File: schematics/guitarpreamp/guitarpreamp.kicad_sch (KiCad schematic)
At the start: 49 parts, among them J1 10k Pot, J10 Conn_01x01_Female, J11 Conn_01x01_Female, J2 Conn_01x08_Female, J3 Conn_01x05_Female, J4 Conn_01x03_Female, U1 9V Linear Regulator, U2 TL072, U3 5V Linear Regulator, U4 3.3v Digital, U5 5v Analog, U6 CS4270-CZZ, X1 SG-5032CAN

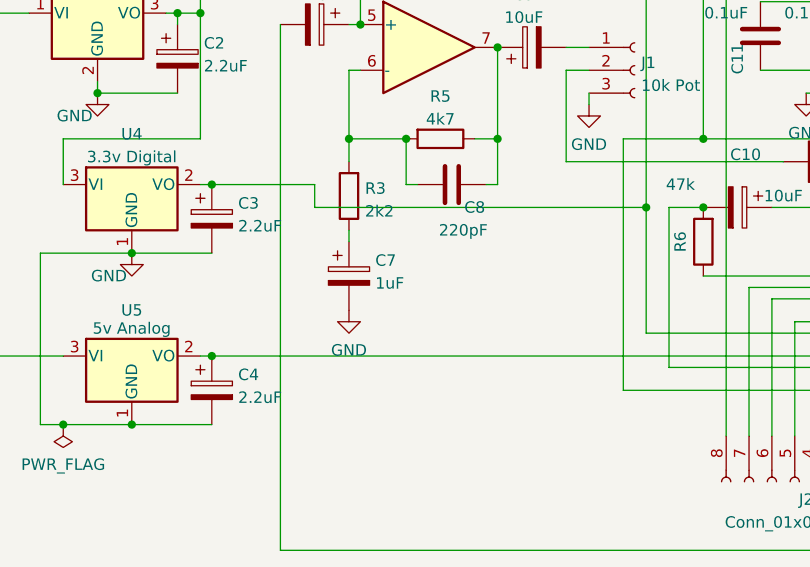
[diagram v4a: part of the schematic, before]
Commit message: changed cab values
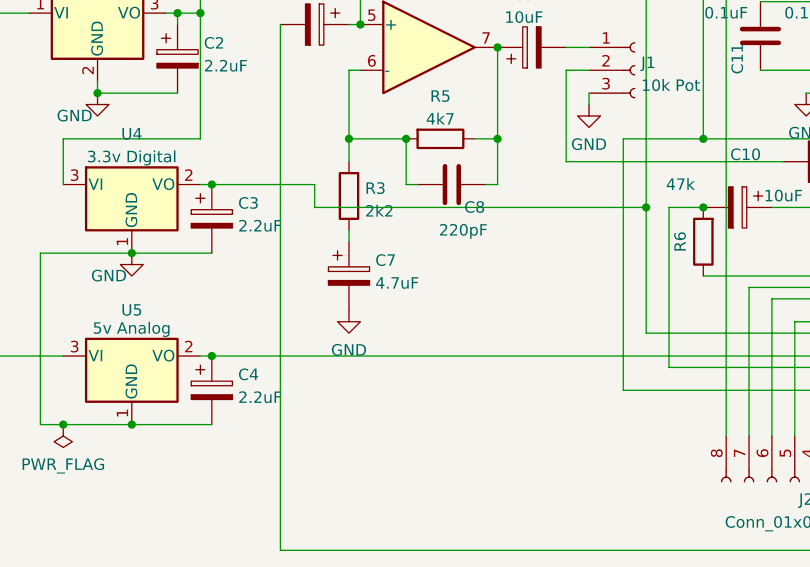
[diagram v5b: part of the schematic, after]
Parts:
- C7: value 1uF -> 4.7uF
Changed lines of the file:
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@@
       (effects (font (size 1.27 1.27)) hide)
     )
-    (pin "1")
-    (pin "2")
-    (pin "3")
-    (pin "5")
-    (pin "6")
-    (pin "7")
     (pin "4")
     (pin "8")
@@
       (effects (font (size 1.27 1.27)) hide)
     )
-    (pin "1")
-    (pin "2")
-    (pin "3")
     (pin "5")
     (pin "6")
     (pin "7")
-    (pin "4")
-    (pin "8")
   )
   (symbol (lib_id "Amplifier_Operational:TL072") (at 90.17 49.53 0) (unit 1)
@@
     (pin "2")
     (pin "3")
-    (pin "5")
-    (pin "6")
-    (pin "7")
-    (pin "4")
-    (pin "8")
   )
   (symbol (lib_id "Device:C_Polarized") (at 233.68 92.71 180) (unit 1)
@@
       (effects (font (size 1.27 1.27)) (justify left))
     )
-    (property "Value" "1uF" (id 1) (at 85.471 101.1432 0)
+    (property "Value" "4.7uF" (id 1) (at 85.471 101.1432 0)
       (effects (font (size 1.27 1.27)) (justify left))
     )
@@
     )
     (path "/cf02f18a-afda-4ef9-b82e-96f662488231"
-      (reference "C7") (unit 1) (value "1uF") (footprint "Capacitor_SMD:CP_Elec_4x4.5")
+      (reference "C7") (unit 1) (value "4.7uF") (footprint "Capacitor_SMD:CP_Elec_4x4.5")
     )
     (path "/5e84eb23-316a-48ca-94bf-3d421a04b84d"

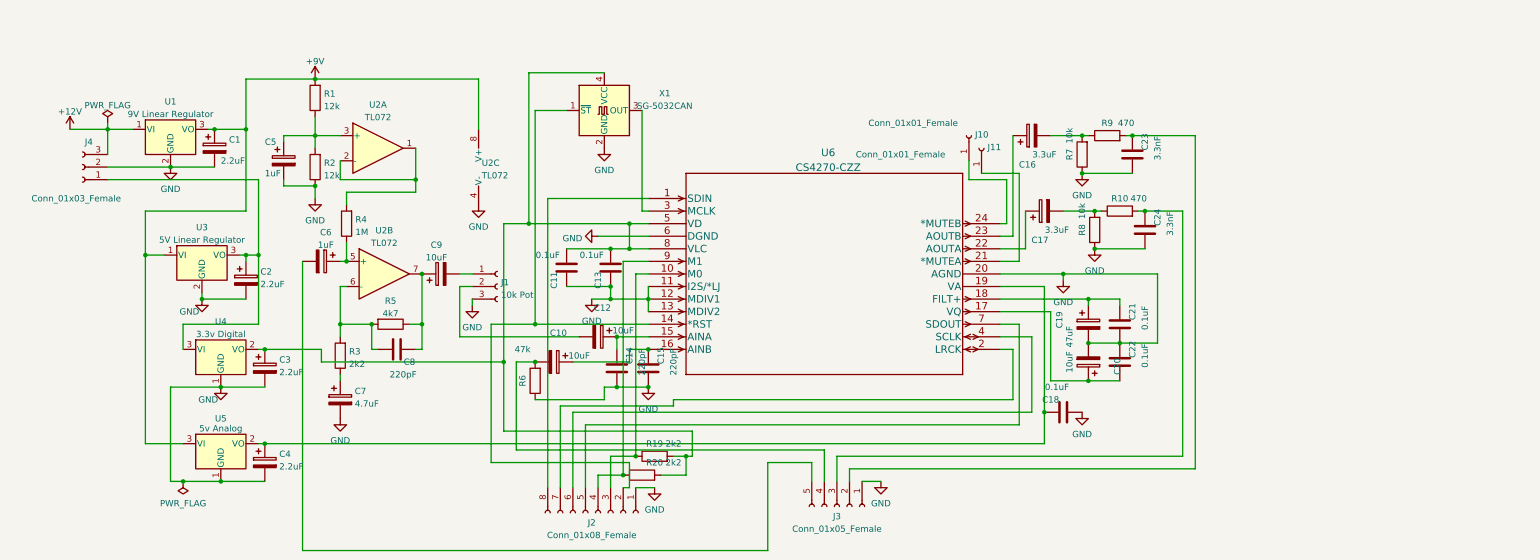
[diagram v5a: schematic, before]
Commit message: schematics changed and added gitignore files
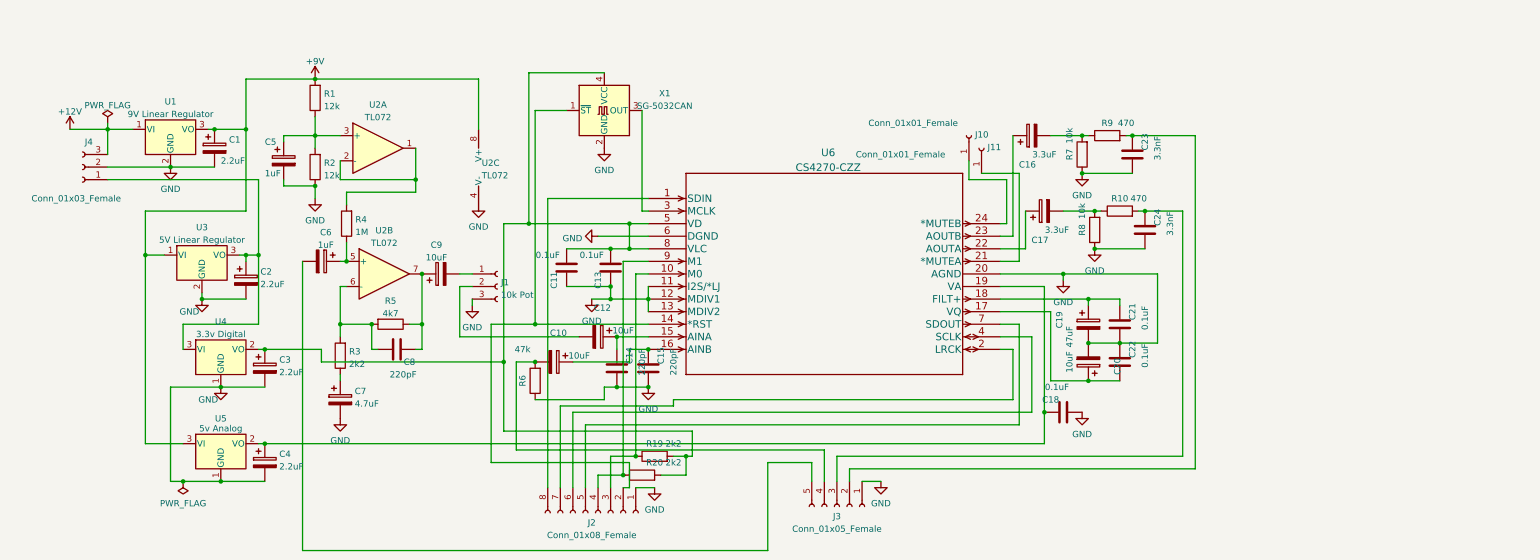
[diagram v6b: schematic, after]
